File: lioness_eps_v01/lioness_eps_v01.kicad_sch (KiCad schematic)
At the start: 0 parts

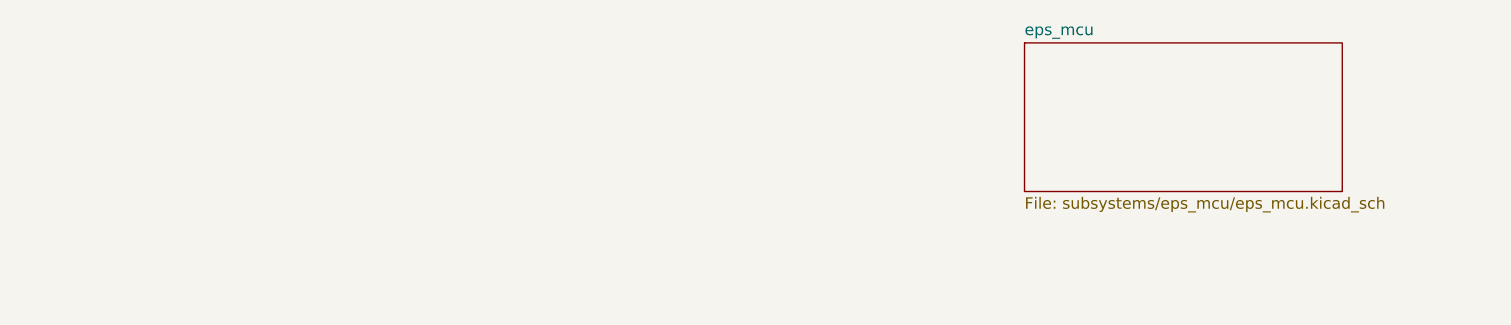
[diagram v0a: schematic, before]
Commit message: added solar board hierarchical sheet
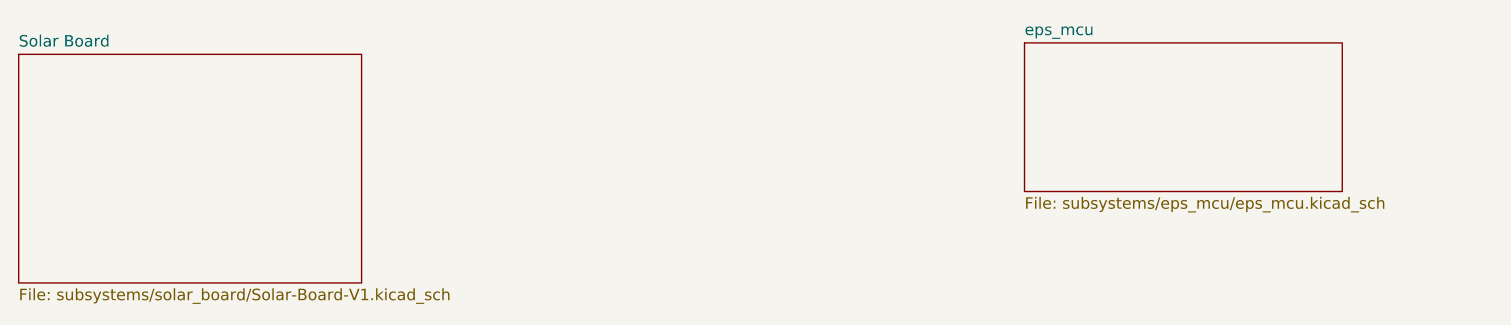
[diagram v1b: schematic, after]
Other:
- added sheet Solar Board (subsystems/solar_board/Solar-Board-V1.kicad_sch)
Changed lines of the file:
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@@
+		)
+	)
+	(sheet
+		(at 76.2 76.2)
+		(size 38.1 25.4)
+		(exclude_from_sim no)
+		(in_bom yes)
+		(on_board yes)
+		(dnp no)
+		(fields_autoplaced yes)
+		(stroke
+			(width 0.1524)
+			(type solid)
+		)
+		(fill
+			(color 0 0 0 0)
+		)
+		(property "Sheetname" "Solar Board"
+			(at 76.2 75.4884 0)
+			(show_name no)
+			(do_not_autoplace no)
+			(effects
+				(font
+					(size 1.27 1.27)
+				)
+				(justify left bottom)
+			)
+		)
+		(property "Sheetfile" "subsystems/solar_board/Solar-Board-V1.kicad_sch"
+			(at 76.2 102.1846 0)
+			(show_name no)
+			(do_not_autoplace no)
+			(effects
+				(font
+					(size 1.27 1.27)
+				)
+				(justify left top)
+			)
+		)
+		(instances
+			(project "lioness_eps_v01"
+				(path "/aa28519f-b679-4a2d-85d7-ece879a7d207"
+					(page "3")
+				)
+			)
 		)
 	)
